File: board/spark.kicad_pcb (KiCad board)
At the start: 4 copper layers, 198 x 85 mm, 132 parts, among them J1 USB_C_Receptacle_USB2.0, J101 Conn_01x01_Shielded, J2 Conn_01x02, J201 Conn_01x01_Shielded, J3 Conn_01x03, J301 Conn_01x01_Shielded, J4 Conn_01x03, J401 Conn_01x01_Shielded, J501 Conn_01x01_Shielded, J601 Conn_01x01_Shielded, P5 Raspberry_Pi_2_3, Q101 Q_NPN_BEC_BRT, Q102 Q_NPN_BEC_BRT, Q201 Q_NPN_BEC_BRT, Q202 Q_NPN_BEC_BRT, Q301 Q_NPN_BEC_BRT, Q302 Q_NPN_BEC_BRT, Q401 Q_NPN_BEC_BRT, Q402 Q_NPN_BEC_BRT, Q501 Q_NPN_BEC_BRT, Q502 Q_NPN_BEC_BRT, Q601 Q_NPN_BEC_BRT, Q602 Q_NPN_BEC_BRT, U1 LD1117S33TR_SOT223, U101 74LVC1G125, U102 TXU0101DCK, U103 SN74LVC1G14DBV, U2 LM317_SOT-223, U201 74LVC1G125, U202 TXU0101DCK, U203 SN74LVC1G14DBV, U301 74LVC1G125, U302 TXU0101DCK, U303 SN74LVC1G14DBV, U401 74LVC1G125, U402 TXU0101DCK, U403 SN74LVC1G14DBV, U501 74LVC1G125, U502 TXU0101DCK, U503 SN74LVC1G14DBV, U601 74LVC1G125, U602 TXU0101DCK, U603 SN74LVC1G14DBV

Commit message: feat: initial board stuff
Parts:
- removed C1, C2, C3, C4: 10uF, Capacitor_SMD:C_0402_1005Metric
- removed C101, C102, C104, C201, C202, C204, C301, C302, C304, C401, C402, C404, C501, C502, C504, C601, C602, C604: 100nF, Capacitor_SMD:C_0402_1005Metric
- removed D101, D201, D301, D401, D501, D601: LED_GREEN, LED_SMD:LED_0603_1608Metric
- removed D102, D202, D302, D402, D502, D602: LED_BLUE, LED_SMD:LED_0603_1608Metric
- removed D103, D203, D303, D403, D503, D603: D_TVS, Resistor_SMD:R_0402_1005Metric
- removed J101, J201, J301, J401, J501, J601: Conn_01x01_Shielded, spark:SMA_LINX_CONSMA002_Horizontal
- removed J3, J4: Conn_01x03, Connector_PinHeader_2.54mm:PinHeader_1x03_P2.54mm_Vertical
- removed Q101, Q102, Q201, Q202, Q301, Q302, Q401, Q402, Q501, Q502, Q601, Q602: Q_NPN_BEC_BRT, Package_TO_SOT_SMD:SOT-323_SC-70
- removed R101, R102, R201, R202, R301, R302, R401, R402, R501, R502, R601, R602: 1K, Resistor_SMD:R_0402_1005Metric
- removed R103, R203, R303, R403, R503, R603: 51, Resistor_SMD:R_0805_2012Metric
- removed R104, R204, R304, R404, R504, R604: 10K, Resistor_SMD:R_0402_1005Metric
- removed Ref** (x6): Val**, spark:raspberry-pi-signal-interface-silks
- removed U101, U201, U301, U401, U501, U601: 74LVC1G125, Package_SO:TSOP-5_1.65x3.05mm_P0.95mm
- removed U102, U202, U302, U402, U502, U602: TXU0101DCK, Package_TO_SOT_SMD:SOT-363_SC-70-6
- removed U103, U203, U303, U403, U503, U603: SN74LVC1G14DBV, Package_TO_SOT_SMD:SOT-23-5
- added D16: Active LED, LED_SMD:LED_0402_1005Metric, F.Cu at (65.0, 125.5)
- added D17: Active LED, LED_SMD:LED_0402_1005Metric, F.Cu at (89.0, 125.5)
- added D2: D_Schottky, Diode_SMD:D_0402_1005Metric, F.Cu at (78.0, 58.5)
- added D3: D_Schottky, Diode_SMD:D_0402_1005Metric, F.Cu at (78.0, 65.5)
- added D4: D_Schottky, Diode_SMD:D_0402_1005Metric, F.Cu at (78.0, 72.5)
- added D5: D_Schottky, Diode_SMD:D_0402_1005Metric, F.Cu at (78.0, 84.5)
- added Q1: AO3400A, Package_TO_SOT_SMD:SOT-23, F.Cu at (74.0, 57.4)
- added Q2: AO3400A, Package_TO_SOT_SMD:SOT-23, F.Cu at (74.0, 64.4)
- added Q22: AO3400A, Package_TO_SOT_SMD:SOT-23, F.Cu at (74.0, 77.9)
- added Q3: AO3400A, Package_TO_SOT_SMD:SOT-23, F.Cu at (74.0, 71.4)
- added Q4: AO3400A, Package_TO_SOT_SMD:SOT-23, F.Cu at (74.0, 83.4)
- added Q5: AO3400A, Package_TO_SOT_SMD:SOT-23, F.Cu at (79.1, 111.0)
- added Q6: AO3400A, Package_TO_SOT_SMD:SOT-23, F.Cu at (87.5, 116.0)
- added R22: 4.7k, Resistor_SMD:R_0402_1005Metric, F.Cu at (145.3, 87.1)
- added R23: 4.7k, Resistor_SMD:R_0402_1005Metric, F.Cu at (145.3, 89.1)
- added R24: 4.7k, Resistor_SMD:R_0402_1005Metric, F.Cu at (145.3, 91.1)
- added R25: 4.7k, Resistor_SMD:R_0402_1005Metric, F.Cu at (145.3, 93.1)
- added R26: 4.7k, Resistor_SMD:R_0402_1005Metric, F.Cu at (148.2, 87.1)
- added R27: 4.7k, Resistor_SMD:R_0402_1005Metric, F.Cu at (148.2, 89.1)
- added R28: 4.7k, Resistor_SMD:R_0402_1005Metric, F.Cu at (148.2, 91.1)
- added R29: 4.7k, Resistor_SMD:R_0402_1005Metric, F.Cu at (148.2, 93.1)
- added R30: 4.7k, Resistor_SMD:R_0402_1005Metric, F.Cu at (151.2, 87.1)
- added R31: 4.7k, Resistor_SMD:R_0402_1005Metric, F.Cu at (151.2, 89.1)
- added R32: 4.7k, Resistor_SMD:R_0402_1005Metric, F.Cu at (83.5, 112.5)
- added R33: 4.7k, Resistor_SMD:R_0402_1005Metric, F.Cu at (84.5, 112.5)
- added R6: 1k, Resistor_SMD:R_0402_1005Metric, F.Cu at (81.5, 111.0)
- added R7: 1k, Resistor_SMD:R_0402_1005Metric, F.Cu at (87.0, 113.5)
- added U11: MAX11614, Package_SO:QSOP-16_3.9x4.9mm_P0.635mm, F.Cu at (41.0, 90.0)
- added U3: LD1117S18TR_SOT223, Package_TO_SOT_SMD:SOT-223-3_TabPin2, F.Cu at (51.5, 47.5)
- added U4: LD1117S25TR_SOT223, Package_TO_SOT_SMD:SOT-223-3_TabPin2, F.Cu at (51.5, 55.8)
- added U5: LD1117S33TR_SOT223, Package_TO_SOT_SMD:SOT-223-3_TabPin2, F.Cu at (51.5, 64.2)
- added U6: LD1117S12TR_SOT223, Package_TO_SOT_SMD:SOT-223-3_TabPin2, F.Cu at (51.5, 72.5)
- added U7: TCA9535DBR, Package_SO:SSOP-24_5.3x8.2mm_P0.65mm, F.Cu at (38.9, 79.5)
- added U8: TXB0104RUT, Package_DFN_QFN:Texas_R-PUQFN-N12, F.Cu at (88.5, 110.0)
- D1: value LED_WHITE -> D_Schottky; footprint LED_SMD:LED_0603_1608Metric -> Diode_SMD:D_0402_1005Metric
- J1: value USB_C_Receptacle_USB2.0 -> RJ45; footprint Connector_USB:USB_C_Receptacle_GCT_USB4105-xx-A_16P_TopMnt_Horizontal -> Connector_RJ:RJ45_Amphenol_54602-x08_Horizontal
- J2: value Conn_01x02 -> RJ45; footprint Connector_PinHeader_2.54mm:PinHeader_2x01_P2.54mm_Vertical -> Connector_RJ:RJ45_Amphenol_54602-x08_Horizontal
- R1: value 1K -> 1k
- R2, R5: value 5.1K -> 1k
- R3: value 220 -> 1k
- R4: value 68 -> 1k
- U1: value LD1117S33TR_SOT223 -> PCA9544APW; footprint Package_TO_SOT_SMD:SOT-223-3_TabPin2 -> Package_SO:TSSOP-20_4.4x6.5mm_P0.65mm
- U2: value LM317_SOT-223 -> PCA9306DC1; footprint Package_TO_SOT_SMD:SOT-223-3_TabPin2 -> Package_SO:VSSOP-8_2.3x2mm_P0.5mm
- moved U1 107.3 mm to (138.1, 100.2), turned to 0 degrees
- moved J2 96.3 mm to (93.9, 117.5)
- moved J1 79.1 mm to (69.9, 117.5), turned to 0 degrees
- moved R1 62.5 mm to (77.0, 76.5)
- moved D1 59.6 mm to (78.0, 79.0)
- moved U2 58.0 mm to (84.5, 110.0), turned to 0 degrees
- moved R5 45.3 mm to (77.0, 82.0), turned to 180 degrees
- moved R3 34.8 mm to (77.0, 63.0), turned to 180 degrees
- moved R2 34.8 mm to (77.0, 56.0), turned to 180 degrees
- moved R4 33.5 mm to (77.0, 70.0), turned to 180 degrees
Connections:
- net iCE_CREST renamed CS_3
- D1 pad 1: GND -> v_bus 1
- D1 pad 2: Net-(D1-Pad2) -> Net-(D1-A)
- J2 pad 1: +3.3V -> GND
- J2 pad 2: +3V3 -> Net-(U8-A1)
- P5 pad 1: +3.3V -> +3V3
- P5 pad 11: PORT1 -> unconnected-(P5-GPIO17-Pad11)
- P5 pad 12: PORT1_TX_ENABLE -> unconnected-(P5-GPIO18/PWM0-Pad12)
- P5 pad 13: PORT2 -> CS_4
- P5 pad 14: GND -> unconnected-(P5-GND-Pad14)
- P5 pad 15: PORT4 -> CS_5
- P5 pad 16: PORT3 -> CS_2
- P5 pad 17: +3.3V -> unconnected-(P5-3V3-Pad17)
- P5 pad 19: iCE_MOSI -> MOSI
- P5 pad 20: GND -> unconnected-(P5-GND-Pad20)
- P5 pad 21: iCE_MISO -> MISO
- P5 pad 22: iCE_CDONE -> unconnected-(P5-GPIO25-Pad22)
- P5 pad 23: iCE_SCK -> SCK
- P5 pad 24: iCE_SS_B -> CS_0
- P5 pad 25: GND -> unconnected-(P5-GND-Pad25)
- P5 pad 26: unconnected-(P5-Pad26) -> CS_1
- P5 pad 29: PORT2_TX_ENABLE -> unconnected-(P5-GCLK1/GPIO5-Pad29)
- P5 pad 3: unconnected-(P5-Pad3) -> SDA
- P5 pad 30: GND -> unconnected-(P5-GND-Pad30)
- P5 pad 31: PORT3_TX_ENABLE -> unconnected-(P5-GCLK2/GPIO6-Pad31)
- P5 pad 32: PORT4_TX_ENABLE -> unconnected-(P5-PWM0/GPIO12-Pad32)
- P5 pad 33: PORT5_TX_ENABLE -> unconnected-(P5-PWM1/GPIO13-Pad33)
- P5 pad 34: GND -> unconnected-(P5-GND-Pad34)
- P5 pad 35: PORT6_TX_ENABLE -> unconnected-(P5-GPIO19/MISO1-Pad35)
- P5 pad 36: PORT5 -> unconnected-(P5-GPIO16-Pad36)
- P5 pad 37: PORT6 -> unconnected-(P5-GPIO26-Pad37)
- P5 pad 38: REMOTE -> unconnected-(P5-GPIO20/MOSI1-Pad38)
- P5 pad 39: GND -> unconnected-(P5-GND-Pad39)
- P5 pad 40: RESET_BTN -> unconnected-(P5-GPIO21/SCLK1-Pad40)
- P5 pad 5: unconnected-(P5-Pad5) -> SCL
- P5 pad 6: GND -> unconnected-(P5-GND-Pad6)
- P5 pad 9: GND -> unconnected-(P5-GND-Pad9)
- R1 pad 1: +3V3 -> bus 1  1.2v
- R1 pad 2: Net-(D1-Pad2) -> GND
- R2 pad 1: Net-(J1-PadA5) -> GND
- R2 pad 2: GND -> bus 1  1.8v
- R3 pad 1: +1V65 -> GND
- R3 pad 2: Net-(R3-Pad2) -> bus 1  2.5v
- R4 pad 1: Net-(R3-Pad2) -> GND
- R4 pad 2: GND -> bus 1  3.3v
- R5 pad 1: Net-(J1-PadB5) -> GND
- R5 pad 2: GND -> bus 1  5v
- U1 pad 1: GND -> unconnected-(U1-A0-Pad1)
- U1 pad 2: +3V3 -> unconnected-(U1-A1-Pad2)
- U1 pad 3: +5V -> unconnected-(U1-A2-Pad3)
- U2 pad 1: Net-(R3-Pad2) -> GND
- U2 pad 2: +1V65 -> v_bus 1
- U2 pad 3: +5V -> Net-(U2-SCL1)
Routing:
- net PORT1: track 166.5 -> 0.00 mm
- net +1V8: track 0.00 -> 166.0 mm
- net +2V5: track 0.00 -> 164.5 mm
- net +1V2: track 0.00 -> 163.0 mm
- net PORT2: track 142.5 -> 0.00 mm
- net PORT3: track 115.6 -> 0.00 mm
- net +3V3: track 55.4 -> 164.2 mm, vias 1 -> 0
- net PORT4: track 94.5 -> 0.00 mm
- net CS_1: track 0.00 -> 86.7 mm, vias 0 -> 1
- net v_bus 1: track 0.00 -> 76.7 mm, vias 0 -> 6
- net PORT5: track 67.7 -> 0.00 mm
- net CS_0: track 0.00 -> 66.3 mm
- net PORT1_TX_ENABLE: track 64.5 -> 0.00 mm
- net Vrx: track 48.9 -> 0.00 mm
- net GND: track 48.5 -> 0.00 mm, vias 0 -> 16
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- added copper zone on In2.Cu, net +5V
- removed copper zone on In2.Cu, net +3V3
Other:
- board text removed: "!!!"
- board text removed: "O"
- board text removed: "Open (default). Closed - !!! U1 3V3 drives pins 1 and 17."
- board text removed: "Q_NPN_BEC_BRT"
- board text removed: "Select output driver voltage 5V | 3.3V"
- board text removed: "Select receiver voltage 1.65V | 3.3V"
- board text removed: "X"
- board text removed: "power"

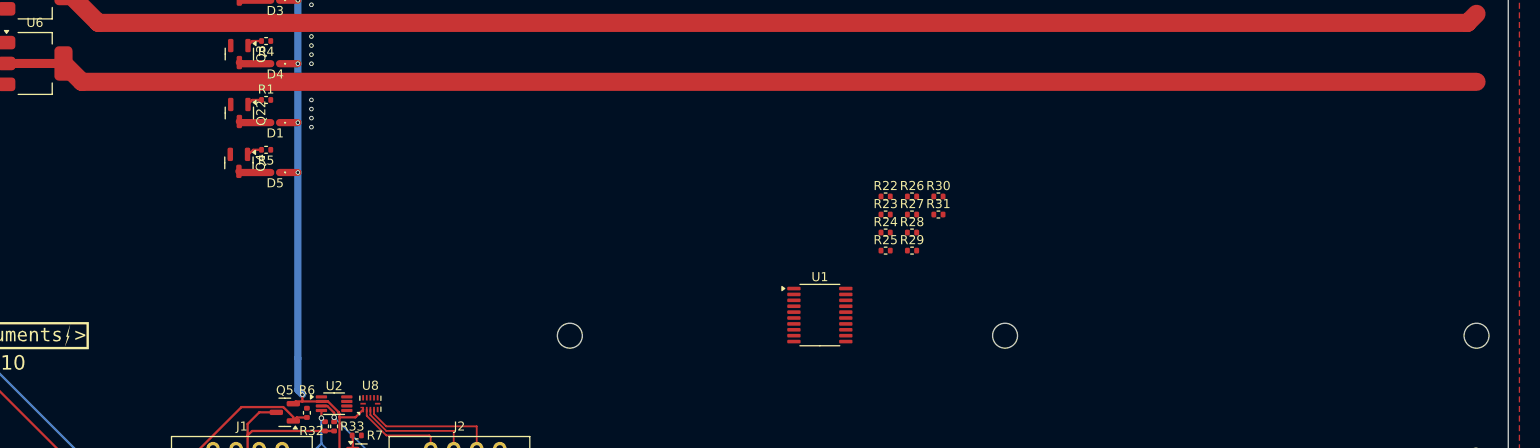
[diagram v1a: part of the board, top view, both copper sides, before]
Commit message: fix: moved mosfets down
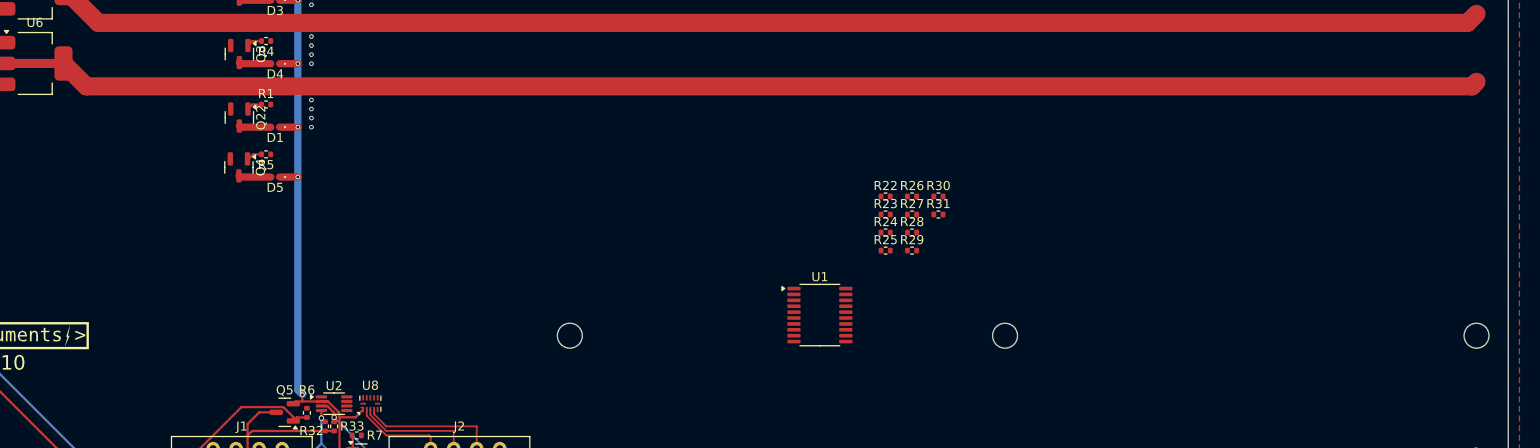
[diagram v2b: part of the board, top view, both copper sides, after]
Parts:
- moved D1 0.50 mm to (78.0, 79.5)
- moved D5 0.50 mm to (78.0, 85.0)
- moved Q22 0.50 mm to (74.0, 78.4)
- moved Q4 0.50 mm to (74.0, 83.9)
- moved R1 0.50 mm to (77.0, 77.0)
- moved R5 0.50 mm to (77.0, 82.5)
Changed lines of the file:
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@@
 	(footprint "Resistor_SMD:R_0402_1005Metric"
 		(layer "F.Cu")
-		(at 77 82 180)
+		(at 77 82.5 180)
 		(descr "Resistor SMD 0402 (1005 Metric), square (rectangular) end terminal, IPC_7351 nominal, (Body size source: IPC-SM-782 page 72, https://www.pcb-3d.com/wordpress/wp-content/uploads/ipc-sm-782a_amendment_1_and_2.pdf), generated with kicad-footprint-generator")
 		(tags "resistor")
@@
 	(footprint "Package_TO_SOT_SMD:SOT-23"
 		(layer "F.Cu")
-		(at 74.05 77.9375 -90)
+		(at 74.05 78.4375 -90)
 		(descr "SOT, 3 Pin (JEDEC TO-236 Var AB https://www.jedec.org/document_search?search_api_views_fulltext=TO-236), generated with kicad-footprint-generator ipc_gullwing_generator.py")
 		(tags "SOT TO_SOT_SMD")
@@
 	(footprint "Diode_SMD:D_0402_1005Metric"
 		(layer "F.Cu")
-		(at 78 84.5 180)
+		(at 78 85 180)
 		(descr "Diode SMD 0402 (1005 Metric), square (rectangular) end terminal, IPC_7351 nominal, (Body size source: http://www.tortai-tech.com/upload/download/2011102023233369053.pdf), generated with kicad-footprint-generator")
 		(tags "diode")
@@
 	(footprint "Diode_SMD:D_0402_1005Metric"
 		(layer "F.Cu")
-		(at 78 79 180)
+		(at 78 79.5 180)
 		(descr "Diode SMD 0402 (1005 Metric), square (rectangular) end terminal, IPC_7351 nominal, (Body size source: http://www.tortai-tech.com/upload/download/2011102023233369053.pdf), generated with kicad-footprint-generator")
 		(tags "diode")
@@
 	(footprint "Package_TO_SOT_SMD:SOT-23"
 		(layer "F.Cu")
-		(at 74 83.4375 -90)
+		(at 74 83.9375 -90)
 		(descr "SOT, 3 Pin (JEDEC TO-236 Var AB https://www.jedec.org/document_search?search_api_views_fulltext=TO-236), generated with kicad-footprint-generator ipc_gullwing_generator.py")
 		(tags "SOT TO_SOT_SMD")
@@
 	(footprint "Resistor_SMD:R_0402_1005Metric"
 		(layer "F.Cu")
-		(at 77 76.5)
+		(at 77 77)
 		(descr "Resistor SMD 0402 (1005 Metric), square (rectangular) end terminal, IPC_7351 nominal, (Body size source: IPC-SM-782 page 72, https://www.pcb-3d.com/wordpress/wp-content/uploads/ipc-sm-782a_amendment_1_and_2.pdf), generated with kicad-footprint-generator")
 		(tags "resistor")
@@
 	)
 	(segment
+		(start 80.5 85)
+		(end 78.485 85)
+		(width 0.8)
+		(layer "F.Cu")
+		(net 4)
+	)
+	(segment
 		(start 78.485 58.5)
 		(end 80.5 58.5)
@@
 	)
 	(segment
-		(start 78.485 79)
-		(end 80.5 79)
-		(width 0.8)
-		(layer "F.Cu")
-		(net 4)
-	)
-	(segment
 		(start 85.097 111.097)
 		(end 85 111)
@@
 	)
 	(segment
-		(start 78.485 84.5)
-		(end 80.5 84.5)
+		(start 78.485 72.5)
+		(end 80.5 72.5)
 		(width 0.8)
 		(layer "F.Cu")
@@
 	)
 	(segment
-		(start 78.485 72.5)
-		(end 80.5 72.5)
+		(start 80.5 79.5)
+		(end 78.485 79.5)
 		(width 0.8)
 		(layer "F.Cu")
@@
 	)
 	(via
-		(at 80.5 84.5)
+		(at 80.5 85)
 		(size 0.5)
 		(drill 0.3)
@@
 	)
 	(via
-		(at 80.5 79)
+		(at 80.5 79.5)
 		(size 0.5)
 		(drill 0.3)
@@
 	)
 	(segment
-		(start 80.5 105)
-		(end 80.5 108.5)
-		(width 0.8)
-		(layer "B.Cu")
-		(net 4)
-	)
-	(segment
-		(start 80.5 72.5)
-		(end 80.5 79)
+		(start 80.5 79.5)
+		(end 80.5 85)
 		(width 0.8)
 		(layer "B.Cu")
@@
 	)
 	(segment
-		(start 80.5 84.5)
-		(end 80.5 105)
+		(start 80.5 108.5)
+		(end 81 109)
 		(width 0.8)
 		(layer "B.Cu")
@@
 	)
 	(segment
-		(start 80.5 79)
-		(end 80.5 84.5)
+		(start 80.5 72.5)
+		(end 80.5 79.5)
 		(width 0.8)
 		(layer "B.Cu")
@@
 	)
 	(segment
-		(start 80.5 108.5)
-		(end 81 109)
+		(start 80.5 85)
+		(end 80.5 108.5)
 		(width 0.8)
 		(layer "B.Cu")
@@
 	)
 	(segment
-		(start 77.515 79)
-		(end 74.175 79)
+		(start 77.515 79.5)
+		(end 74.175 79.5)
 		(width 0.8)
 		(layer "F.Cu")
@@
 	)
 	(segment
-		(start 74.175 79)
-		(end 74.05 78.875)
+		(start 74.175 79.5)
+		(end 74.05 79.375)
 		(width 0.8)
 		(layer "F.Cu")
@@
 	)
 	(segment
-		(start 77.515 84.5)
-		(end 74.125 84.5)
+		(start 77.515 85)
+		(end 74.125 85)
 		(width 0.8)
 		(layer "F.Cu")
@@
 	)
 	(segment
-		(start 74.125 84.5)
-		(end 74 84.375)
+		(start 74.125 85)
+		(end 74 84.875)
 		(width 0.8)
 		(layer "F.Cu")
@@
 	)
 	(segment
-		(start 54.65 72.475)
-		(end 56.675 74.5)
+		(start 210 75)
+		(end 210.5 74.5)
 		(width 2)
 		(layer "F.Cu")
@@
 	)
 	(segment
-		(start 56.675 74.5)
-		(end 210.5 74.5)
+		(start 57.175 75)
+		(end 210 75)
+		(width 2)
+		(layer "F.Cu")
+		(net 58)
+	)
+	(segment
+		(start 54.65 72.475)
+		(end 57.175 75)
 		(width 2)
 		(layer "F.Cu")
@@
 	)
 	(segment
-		(start 75.5 76.5)
-		(end 75 77)
+		(start 75.5 77)
+		(end 75 77.5)
 		(width 0.254)
 		(layer "F.Cu")
@@
 	)
 	(segment
-		(start 76.49 76.5)
-		(end 75.5 76.5)
+		(start 76.49 77)
+		(end 75.5 77)
 		(width 0.254)
 		(layer "F.Cu")
@@
 	)
 	(segment
-		(start 75.575 82)
-		(end 74.95 82.625)
+		(start 75.575 82.5)
+		(end 74.95 83.125)
 		(width 0.254)
 		(layer "F.Cu")
@@
 	)
 	(segment
-		(start 76.49 82)
-		(end 75.575 82)
+		(start 76.49 82.5)
+		(end 75.575 82.5)
 		(width 0.254)
 		(layer "F.Cu")

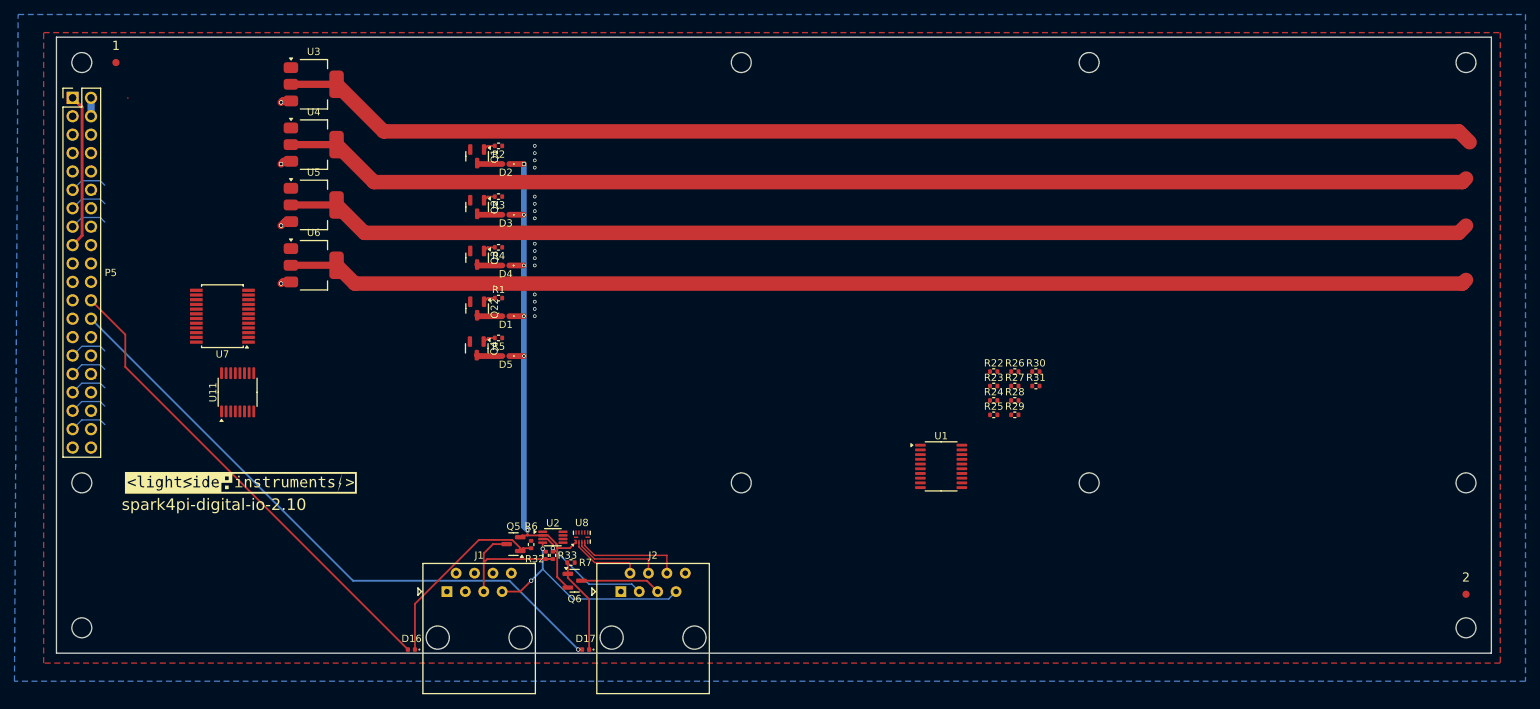
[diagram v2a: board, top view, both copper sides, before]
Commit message: feat: connected mosfets
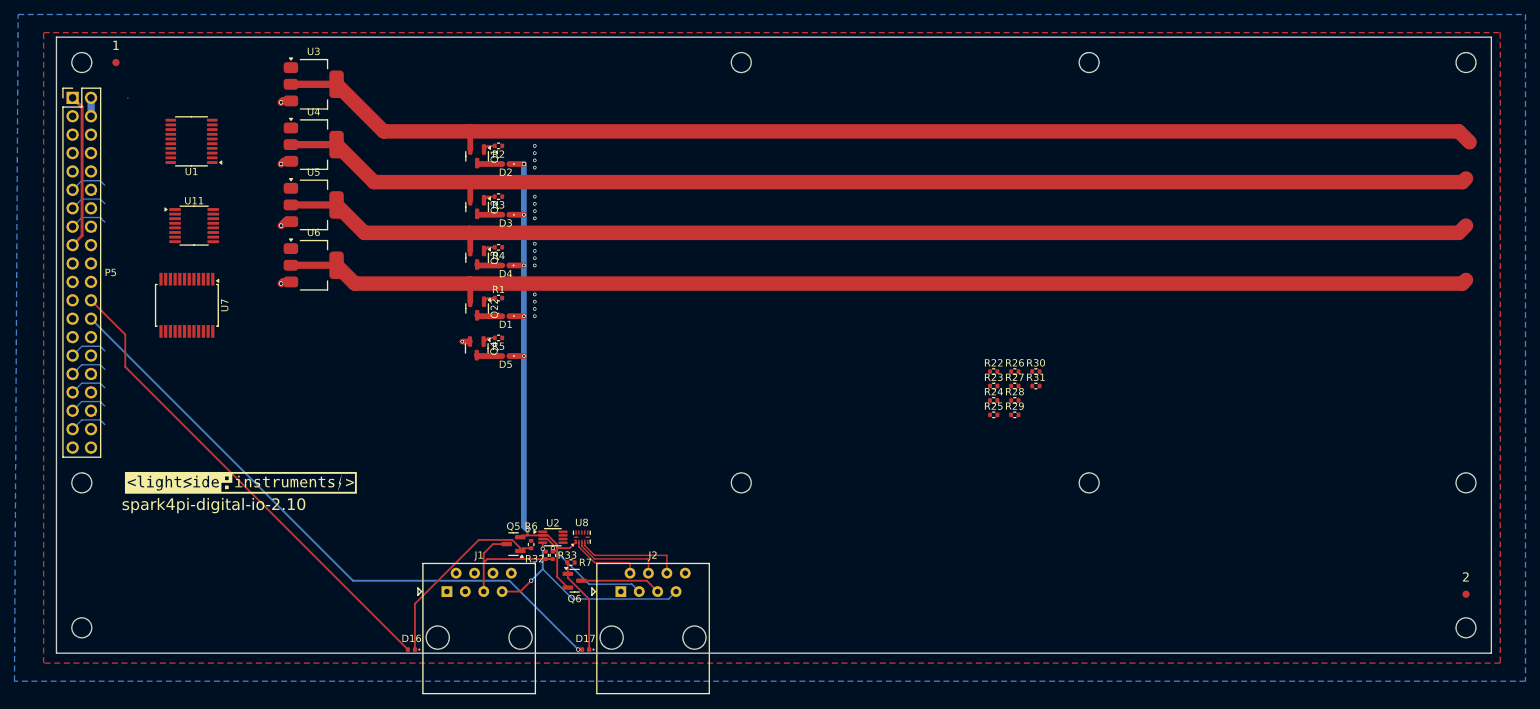
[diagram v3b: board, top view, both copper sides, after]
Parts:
- moved U1 112.7 mm to (34.6, 55.4), turned to 180 degrees
- moved U11 23.8 mm to (35.0, 67.0), turned to 0 degrees
- moved U7 5.12 mm to (34.0, 78.0), turned to -90 degrees
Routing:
- net +3V3: track 164.2 -> 166.7 mm
- net +1V8: track 166.0 -> 168.5 mm
- net +1V2: track 163.4 -> 165.9 mm
- net +2V5: track 164.5 -> 167.0 mm
- net +5V: track 8.50 -> 9.55 mm, vias 4 -> 5

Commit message: feat: updated version number
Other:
- board text added: "spark4pi-signals-0.1"
- board text removed: "spark4pi-digital-io-2.10"
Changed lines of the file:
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@@
 		(layer "Edge.Cuts")
 	)
-	(gr_text "spark4pi-digital-io-2.10"
+	(gr_text "spark4pi-signals-0.1"
 		(at 25 105.5 0)
 		(layer "F.SilkS")

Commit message: feat: inital version
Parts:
- moved R28 129.6 mm to (26.0, 48.0), turned to -90 degrees
- moved R29 129.4 mm to (27.0, 48.0), turned to -90 degrees
- moved R30 129.2 mm to (28.0, 48.0), turned to -90 degrees
- moved R31 128.9 mm to (29.0, 48.0), turned to -90 degrees
- moved R27 126.1 mm to (26.0, 58.0), turned to 90 degrees
- moved R26 124.7 mm to (27.0, 58.0), turned to 90 degrees
- moved R25 122.5 mm to (28.0, 58.0), turned to 90 degrees
- moved R24 121.0 mm to (29.0, 58.0), turned to 90 degrees
- moved R23 119.5 mm to (30.0, 58.0), turned to 90 degrees
- moved R22 118.0 mm to (31.0, 58.0), turned to 90 degrees
- moved U6 25.0 mm to (51.5, 47.5)
- moved D1 20.9 mm to (78.0, 58.6)
- moved Q22 20.9 mm to (74.0, 57.5)
- moved R1 20.9 mm to (77.0, 56.1)
- moved U7 16.4 mm to (38.4, 62.2), turned to 180 degrees
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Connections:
- U7 pad 4: bus 1  1.2v -> bus 1  5v
- U7 pad 5: bus 1  1.8v -> bus 1  3.3v
- U7 pad 7: bus 1  3.3v -> bus 1  1.8v
- U7 pad 8: bus 1  5v -> bus 1  1.2v
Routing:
- net +2V5: track 167.0 -> 42.5 mm
- net +1V8: track 168.5 -> 44.2 mm
- net +3V3: track 166.7 -> 44.5 mm, vias 0 -> 4
- net +1V2: track 165.9 -> 43.7 mm
- net MOSI: track 0.00 -> 107.5 mm, vias 0 -> 1
- net MISO: track 0.00 -> 105.9 mm, vias 0 -> 1
- net SCK: track 0.00 -> 104.7 mm, vias 0 -> 1
- net bus 1 a 2: track 0.00 -> 90.9 mm, vias 0 -> 1
- net SDA 0: track 0.00 -> 90.8 mm, vias 0 -> 2
- net SCL 0: track 0.00 -> 86.2 mm, vias 0 -> 2
- net bus 1 a 1: track 0.00 -> 66.5 mm, vias 0 -> 1
- net bus 1  5v: track 1.80 -> 45.4 mm, vias 0 -> 2
- net bus 1  3.3v: track 1.45 -> 40.9 mm, vias 0 -> 2
- net bus 1  2.5v: track 1.70 -> 38.6 mm, vias 0 -> 2
- net bus 1  1.2v: track 1.70 -> 37.6 mm, vias 0 -> 2
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- added copper zone on In1.Cu, net +3V3
- removed copper zone on In1.Cu, net GND
